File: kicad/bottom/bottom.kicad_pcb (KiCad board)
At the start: 2 copper layers, 65 x 120 mm, 17 parts, among them J1 Conn_01x15_Socket

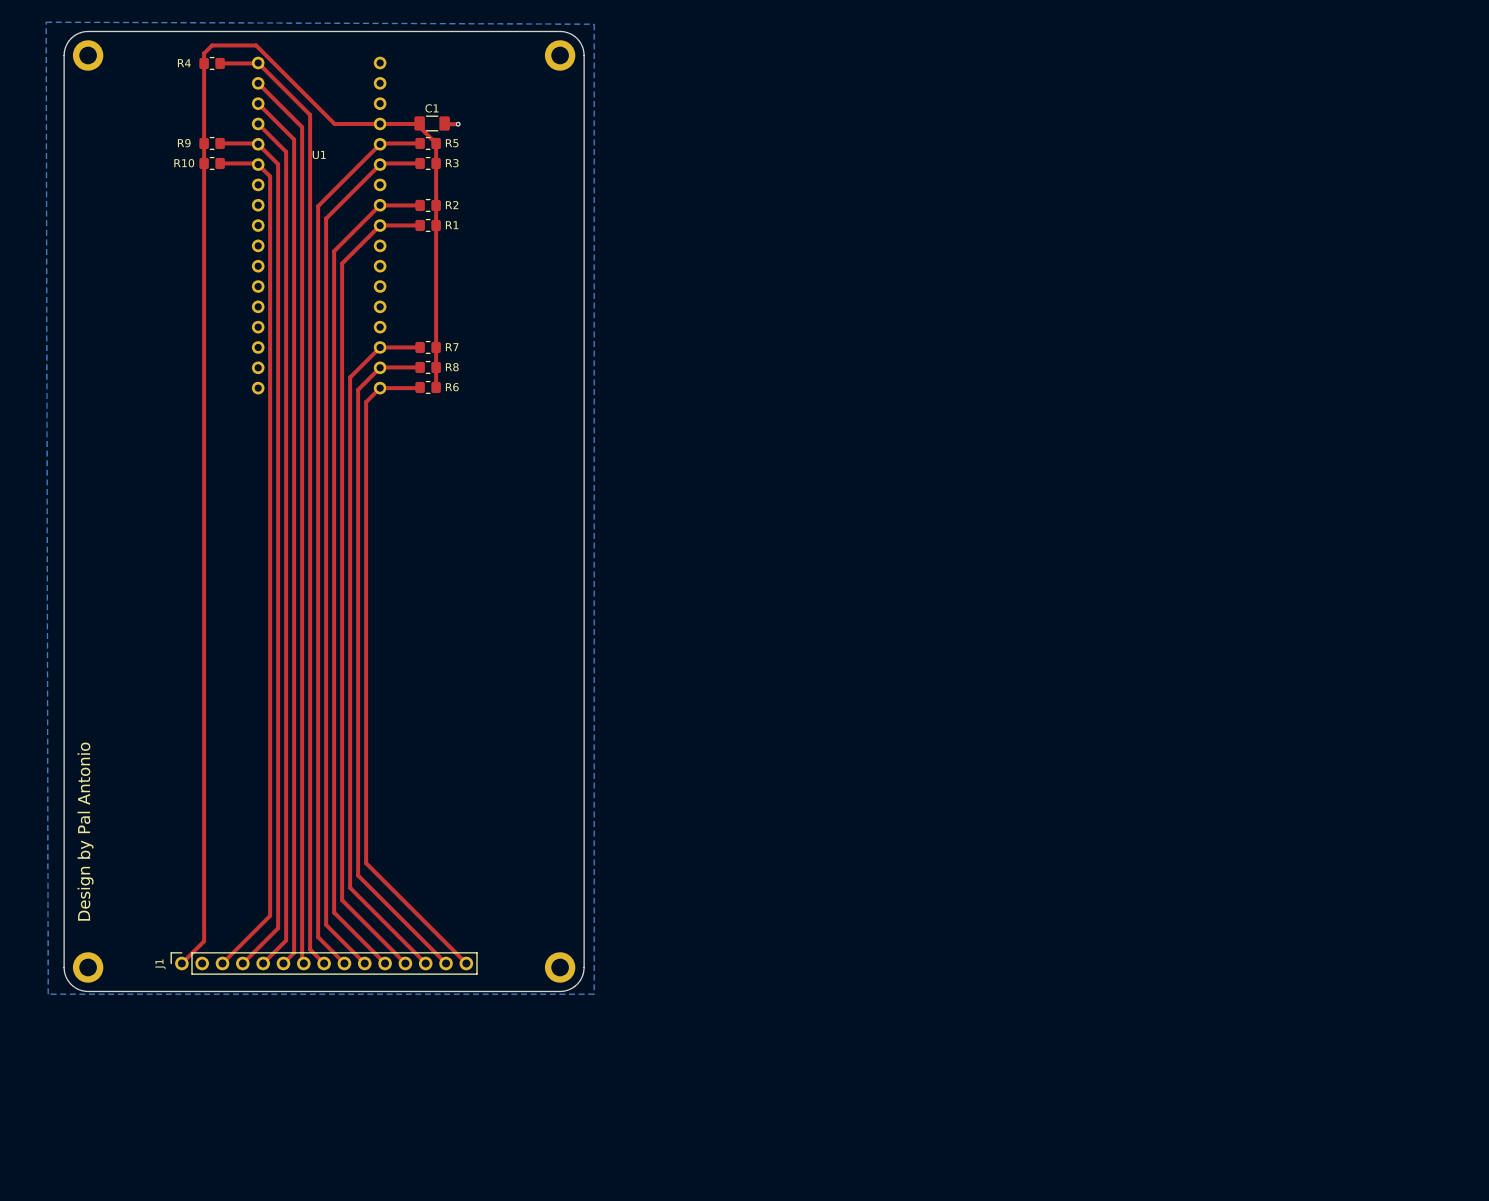
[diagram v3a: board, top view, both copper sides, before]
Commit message: update imports, readme, documentatie, add 10 addressable rgbs
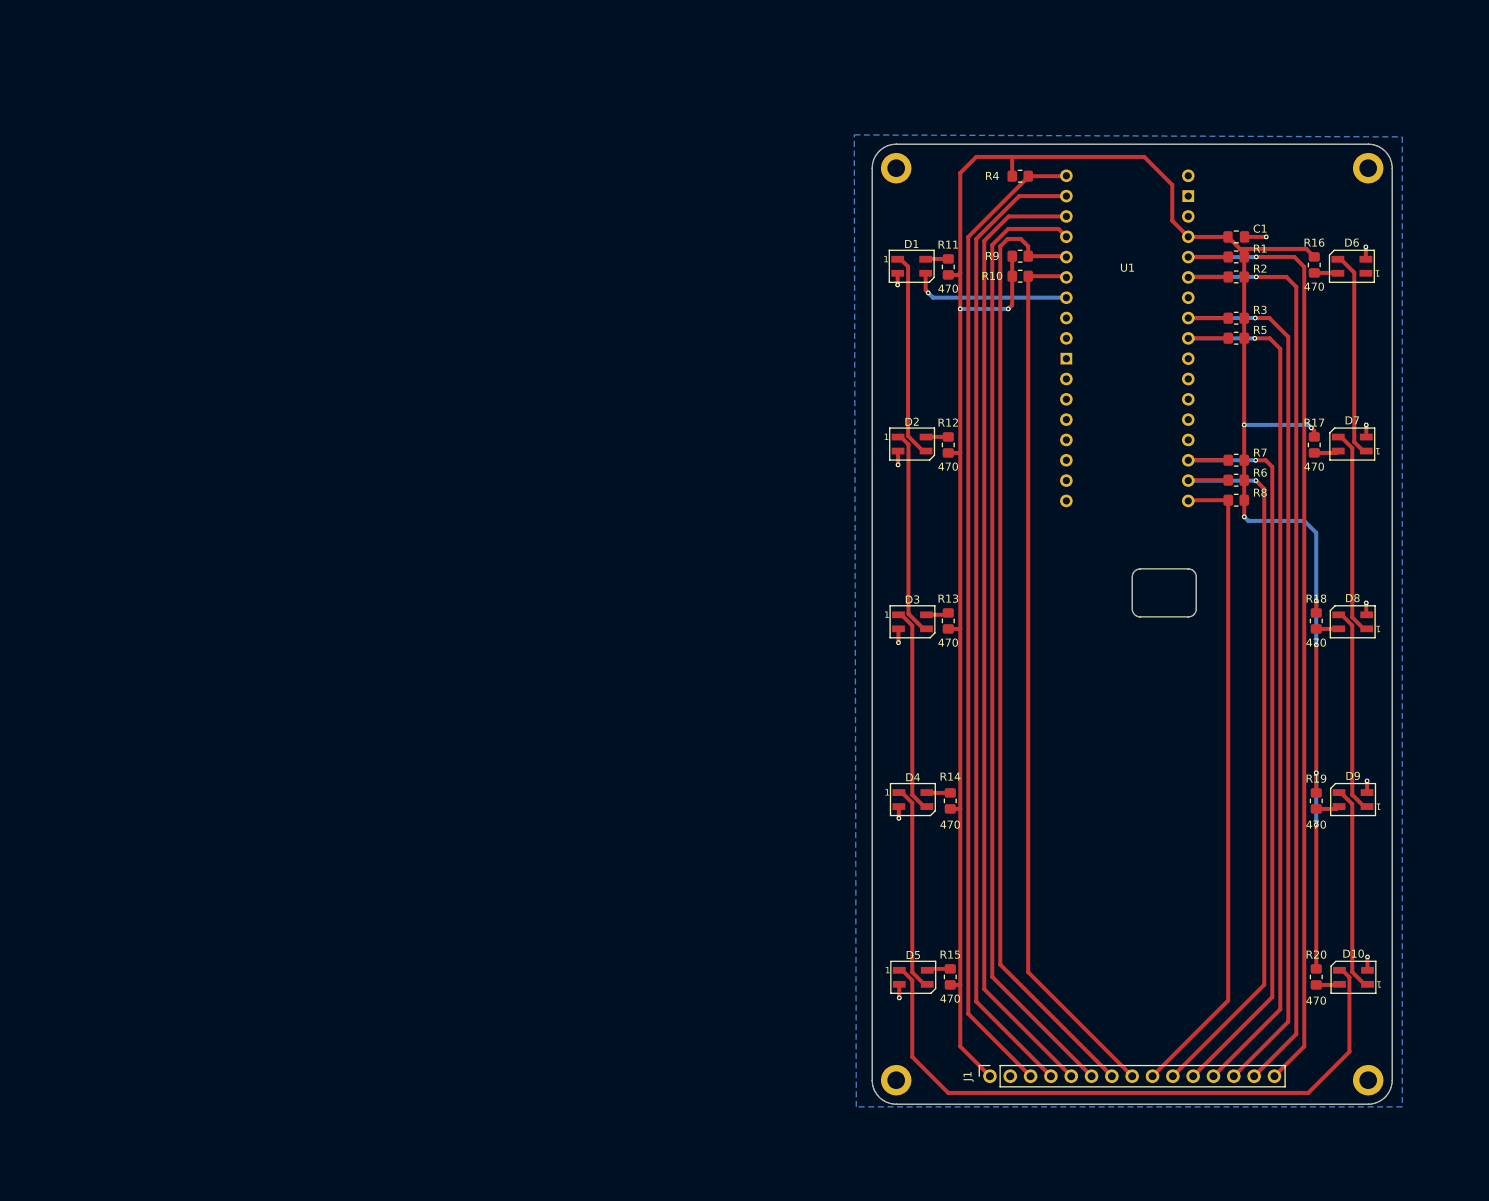
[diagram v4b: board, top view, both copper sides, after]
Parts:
- added D1: SK6812MINI, Bottom-Footprints:LED_SK6812MINI_PLCC4_3.5x3.5mm_P1.75mm, F.Cu at (124.9, 44.3)
- added D10: SK6812MINI, Bottom-Footprints:LED_SK6812MINI_PLCC4_3.5x3.5mm_P1.75mm, F.Cu at (180.2, 133.1)
- added D2: SK6812MINI, Bottom-Footprints:LED_SK6812MINI_PLCC4_3.5x3.5mm_P1.75mm, F.Cu at (125.0, 66.5)
- added D3: SK6812MINI, Bottom-Footprints:LED_SK6812MINI_PLCC4_3.5x3.5mm_P1.75mm, F.Cu at (125.0, 88.7)
- added D4: SK6812MINI, Bottom-Footprints:LED_SK6812MINI_PLCC4_3.5x3.5mm_P1.75mm, F.Cu at (125.1, 110.9)
- added D5: SK6812MINI, Bottom-Footprints:LED_SK6812MINI_PLCC4_3.5x3.5mm_P1.75mm, F.Cu at (125.1, 133.1)
- added D6: SK6812MINI, Bottom-Footprints:LED_SK6812MINI_PLCC4_3.5x3.5mm_P1.75mm, F.Cu at (180.0, 44.3)
- added D7: SK6812MINI, Bottom-Footprints:LED_SK6812MINI_PLCC4_3.5x3.5mm_P1.75mm, F.Cu at (180.0, 66.5)
- added D8: SK6812MINI, Bottom-Footprints:LED_SK6812MINI_PLCC4_3.5x3.5mm_P1.75mm, F.Cu at (180.1, 88.7)
- added D9: SK6812MINI, Bottom-Footprints:LED_SK6812MINI_PLCC4_3.5x3.5mm_P1.75mm, F.Cu at (180.1, 110.9)
- added G***: LOGO, Bottom-Footprints:nubcat4_24mm, B.Cu at (152.5, 109.6)
- added G***: LOGO, Bottom-Footprints:nubcat_24mm, B.Cu at (151.5, 127.1)
- added G***: LOGO, Bottom-Footprints:nubcat_24mm, B.Cu at (151.6, 92.6)
- added R11: 470, Bottom-Footprints:R_0805_2012Metric_Pad1.20x1.40mm_HandSolder, F.Cu at (129.5, 44.3)
- added R12: 470, Bottom-Footprints:R_0805_2012Metric_Pad1.20x1.40mm_HandSolder, F.Cu at (129.5, 66.6)
- added R13: 470, Bottom-Footprints:R_0805_2012Metric_Pad1.20x1.40mm_HandSolder, F.Cu at (129.5, 88.6)
- added R14: 470, Bottom-Footprints:R_0805_2012Metric_Pad1.20x1.40mm_HandSolder, F.Cu at (129.8, 111.1)
- added R15: 470, Bottom-Footprints:R_0805_2012Metric_Pad1.20x1.40mm_HandSolder, F.Cu at (129.8, 133.1)
- added R16: 470, Bottom-Footprints:R_0805_2012Metric_Pad1.20x1.40mm_HandSolder, F.Cu at (175.3, 44.1)
- added R17: 470, Bottom-Footprints:R_0805_2012Metric_Pad1.20x1.40mm_HandSolder, F.Cu at (175.3, 66.6)
- added R18: 470, Bottom-Footprints:R_0805_2012Metric_Pad1.20x1.40mm_HandSolder, F.Cu at (175.5, 88.6)
- added R19: 470, Bottom-Footprints:R_0805_2012Metric_Pad1.20x1.40mm_HandSolder, F.Cu at (175.5, 111.1)
- added R20: 470, Bottom-Footprints:R_0805_2012Metric_Pad1.20x1.40mm_HandSolder, F.Cu at (175.5, 133.1)
- C1: footprint Bottom-Footprints:C_1206_3216Metric_Pad1.33x1.80mm_HandSolder -> Bottom-Footprints:C_0805_2012Metric_Pad1.18x1.45mm_HandSolder
- moved R5 103.9 mm to (165.5, 53.2)
- moved R3 102.8 mm to (165.5, 50.8)
- moved R8 102.4 mm to (165.5, 73.5)
- moved U1 102.0 mm to (151.9, 53.3)
- moved H1 102.0 mm to (123.0, 32.0)
- moved H2 102.0 mm to (182.0, 32.0)
- moved H3 102.0 mm to (182.0, 146.0)
- moved H4 102.0 mm to (123.0, 146.0)
- moved R7 102.0 mm to (165.5, 68.5)
- moved J1 102.0 mm to (134.7, 145.5)
- moved R10 102.0 mm to (138.5, 45.5)
- moved R4 102.0 mm to (138.5, 33.0)
- moved R9 102.0 mm to (138.5, 43.0)
- moved R6 101.7 mm to (165.5, 71.0)
- moved C1 101.5 mm to (165.5, 40.6)
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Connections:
- J1 pad 10: ROW2 -> ENC_CLK
- J1 pad 11: ROW1 -> ENC_DT
- J1 pad 12: ROW0 -> ROW3
- J1 pad 13: ENC_DT -> ROW2
- J1 pad 14: ENC_SW -> ROW1
- J1 pad 15: ENC_CLK -> ROW0
- J1 pad 3: OLED_SDA -> BT_SELECT
- J1 pad 4: OLED_SCL -> COL0
- J1 pad 5: COL0 -> COL1
- J1 pad 6: COL1 -> COL2
- J1 pad 7: COL2 -> OLED_SCL
- J1 pad 8: BT_SELECT -> OLED_SDA
- J1 pad 9: ROW3 -> ENC_SW
- U1 pad 16: ENC_SW -> ENC_CLK
- U1 pad 17: ENC_CLK -> ENC_SW
- U1 pad 28: unconnected-(U1-7-Pad28) -> RGB_LEDS
- U1 pad 31: COL0 -> COL2
- U1 pad 33: COL2 -> COL0
- U1 pad 5: ROW3 -> ROW0
- U1 pad 6: ROW2 -> ROW1
- U1 pad 8: ROW1 -> ROW2
- U1 pad 9: ROW0 -> ROW3
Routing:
- net +3.3V: track 179.7 -> 303.8 mm, vias 0 -> 9
- net Net-(D10-DIN): track 0.00 -> 81.3 mm
- net Net-(D7-DIN): track 0.00 -> 25.9 mm
- net Net-(D8-DIN): track 0.00 -> 25.9 mm
- net Net-(D6-DIN): track 0.00 -> 25.9 mm
- net Net-(D10-DOUT): track 0.00 -> 25.8 mm
- net Net-(D1-DOUT): track 0.00 -> 25.1 mm
- net Net-(D3-DOUT): track 0.00 -> 25.1 mm
- net Net-(D2-DOUT): track 0.00 -> 25.1 mm
- net Net-(D4-DOUT): track 0.00 -> 25.1 mm
- net ROW0: track 102.5 -> 122.7 mm, vias 0 -> 1
- net RGB_LEDS: track 0.00 -> 20.1 mm, vias 0 -> 1
- net GND: track 1.73 -> 18.5 mm, vias 1 -> 11
- net ROW1: track 104.8 -> 119.9 mm, vias 0 -> 1
- net COL0: track 107.6 -> 122.0 mm
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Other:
- outline, holes or cut-outs redrawn
- board text removed: "Design by Pal Antonio"

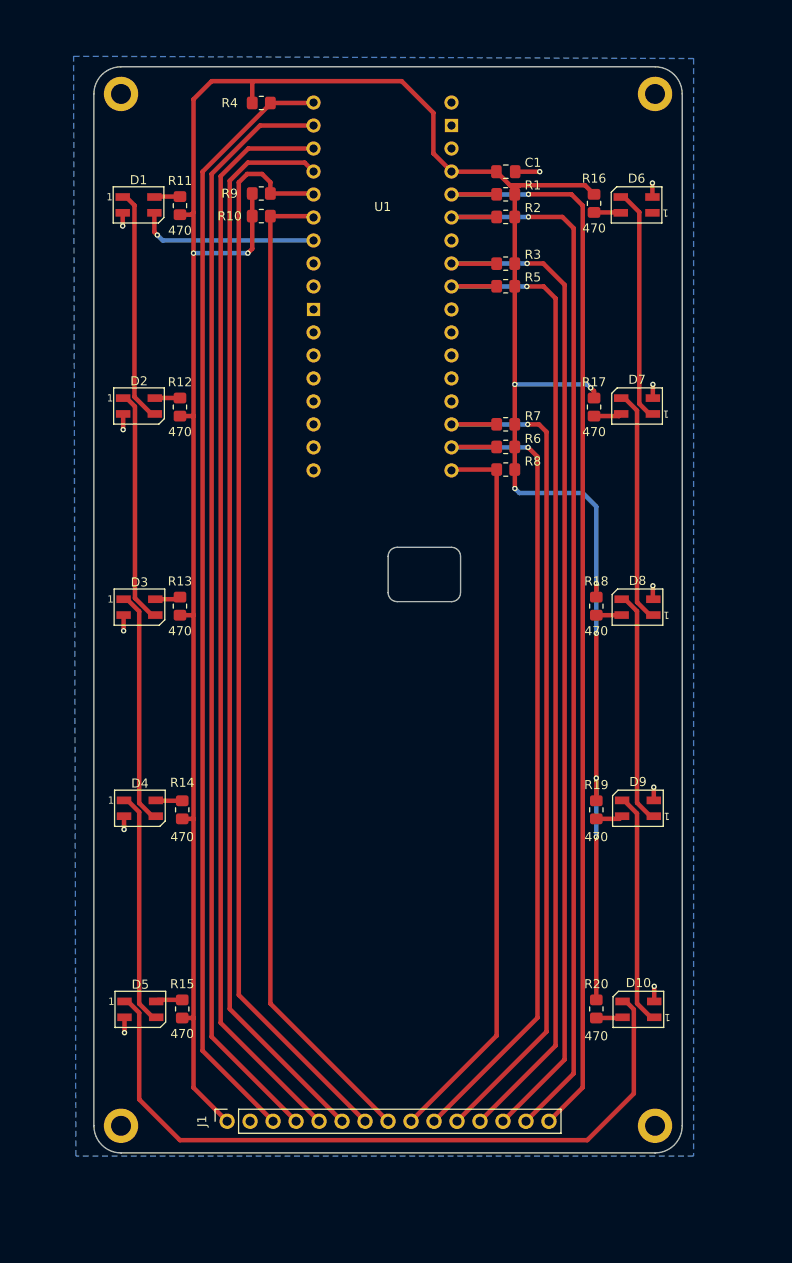
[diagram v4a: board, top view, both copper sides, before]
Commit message: Update KiCad project files and documentation
- Adjusted pad dimensions in top.kicad_pro:
  - Drill size changed from 1.0 to 0.8
  - Height changed from 1.7 to 1.6
  - Width changed from 1.7 to 2.0
- Modified design rule for isolated copper from "warning" to "ignore"
- Increased minimum hole clearance from 0.16 to 0.25

- Corrected global label positions for OLED_SDA and OLED_SCL in top.kicad_sch
- Updated footprint properties for mounting holes in top.kicad_sch to "MountingHole:MountingHole_2.5mm_Pad"

- Created new documentation file for component details.
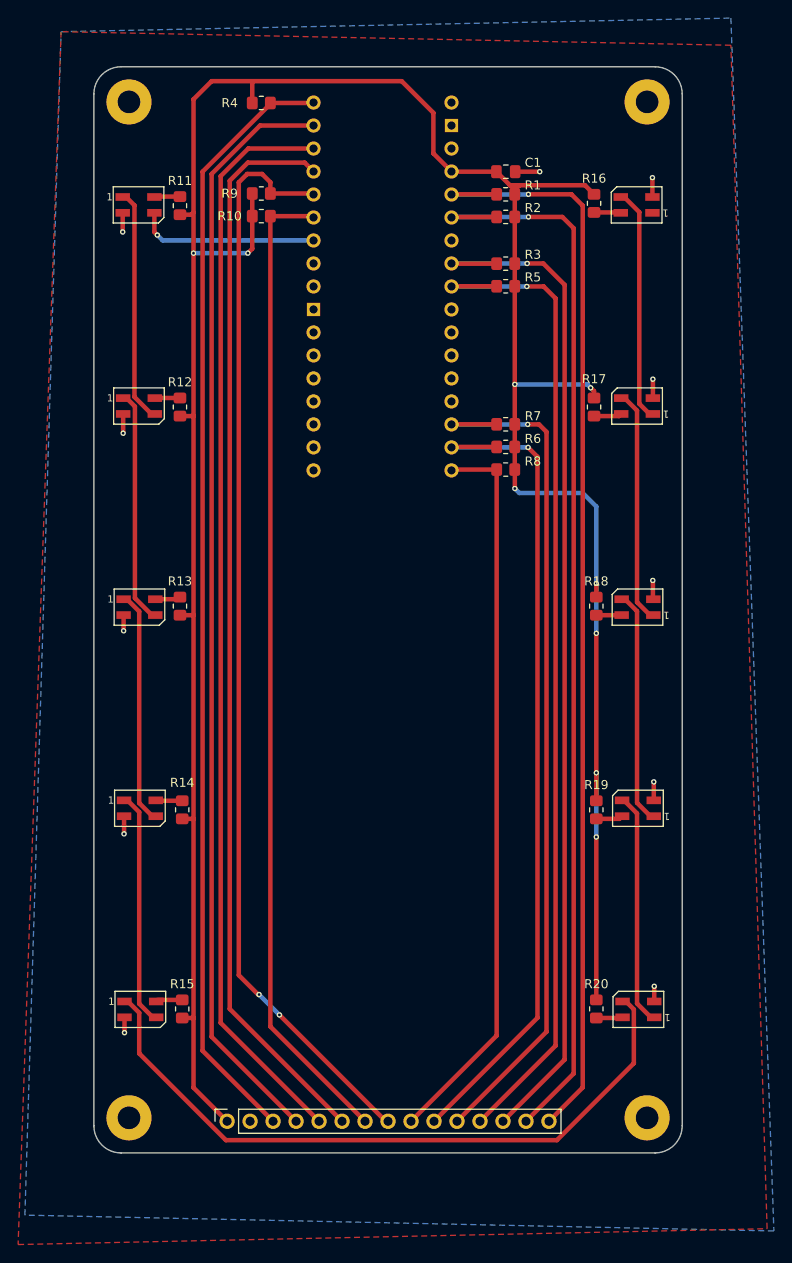
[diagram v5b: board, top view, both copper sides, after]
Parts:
- removed the G*** at (152.5, 109.6)
- removed the G*** at (151.6, 92.6)
- H1, H2, H3, H4: footprint Bottom-Footprints:MountingHole_2.2mm_M2_DIN965_Pad -> MountingHole:MountingHole_2.5mm_Pad
- moved G*** 3.10 mm to (152.0, 124.0)
- moved H1 1.24 mm to (123.9, 32.9)
- moved H2 1.24 mm to (181.1, 32.9)
- moved H3 1.24 mm to (181.1, 145.1)
- moved H4 1.24 mm to (123.9, 145.1)
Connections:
- J1 pad 7: OLED_SCL -> OLED_SDA
- J1 pad 8: OLED_SDA -> OLED_SCL
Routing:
- net Net-(D10-DIN): track 81.3 -> 75.6 mm
- net GND: track 18.5 -> 22.3 mm
- net OLED_SCL: track 119.7 -> 121.0 mm, vias 0 -> 2
- net OLED_SDA: track 110.0 -> 109.0 mm
- net Net-(D8-DIN): track 25.9 -> 25.1 mm
- net Net-(D7-DIN): track 25.9 -> 25.1 mm
- net Net-(D6-DIN): track 25.9 -> 25.1 mm
- net Net-(D10-DOUT): track 25.8 -> 25.2 mm
- net +3.3V: track 303.8 -> 304.3 mm
- added copper zone on F.Cu, net GND
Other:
- outline, holes or cut-outs redrawn

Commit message: removed scottokeebs kicad files, updated the mounting holes to use m2.5 instead of m2, added m2.5 footprints to each pcbs footprint library
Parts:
- H1, H2, H3, H4: footprint MountingHole:MountingHole_2.5mm_Pad -> Bottom-Footprints:MountingHole_2.5mm_Pad
